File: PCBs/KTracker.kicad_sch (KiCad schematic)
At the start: 63 parts, among them J1 Conn_01x02_Female, J2 Conn_01x04_Female, J3 Conn_01x02_Female, J4 Conn_01x08_Female, J5 Conn_01x02_Female, P1 USB_C_Plug_USB2.0, SW1 Option/FLASH Switch, SW2 Cali Switch, SW3 SW_SPDT MAIN POWER, U1 ME6211C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

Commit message: #auto_saved_files#
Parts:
- added U?: MPU-9250, Sensor_Motion:InvenSense_QFN-24_3x3mm_P0.4mm, symbol Sensor_Motion:MPU-9250
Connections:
- net +3V3: no longer R11.1, R12.1
- net AUX_SCL: now also U?.7 (AUX_SCL); no longer U3.7 (AUX_SCL)
- net AUX_SDA: now also U?.21 (AUX_SDA); no longer U3.6 (AUX_SDA)
- net GND: now also U?.18 (GND), U?.20 (RESV_GND); no longer C8.2, U3.18 (GND)
- net SCL: now also U?.23 (SCL/SCLK); no longer U3.23 (SCL)
- net SDA: now also U?.24 (SDA/MOSI); no longer U3.24 (SDA)
- net at U3.10 (REGOUT): no longer C7.1
- net at U3.11 (FSYNC), U3.9 (AD0): no longer R16.1
- net at U3.20 (CPOUT): no longer C8.1
- new net: R16.1, U?.11 (FSYNC), U?.9 (AD0/MISO)
- new net: C7.1, U?.10 (REGOUT)
- new net: R11.1, R12.1, U?.13 (VDD), U?.22 (~{CS}), U?.8 (VDDIO)
- no-connect marks 33 -> 35
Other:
- moved on the sheet: C7, C8, R11, R12, R16

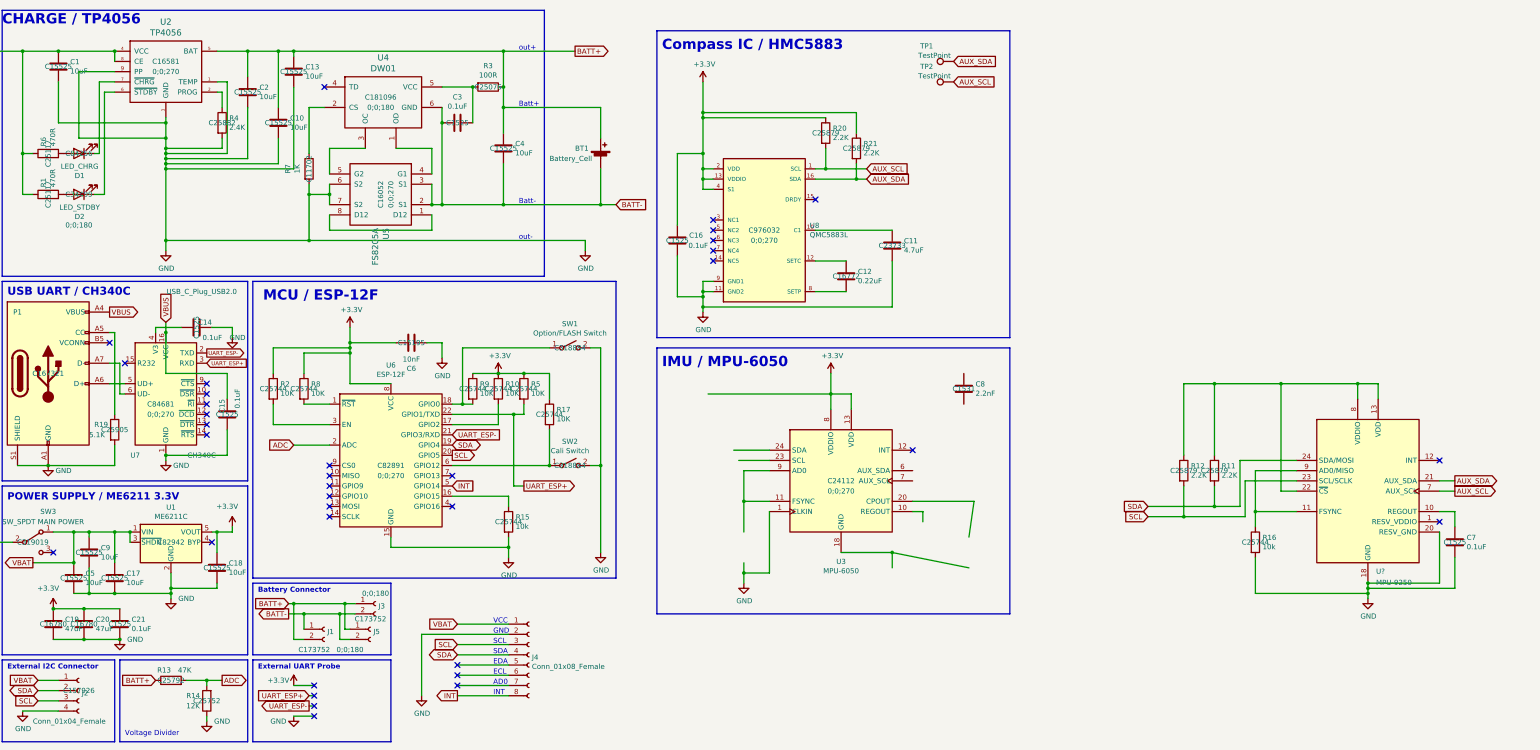
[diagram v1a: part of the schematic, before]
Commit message: MPU 6500!!
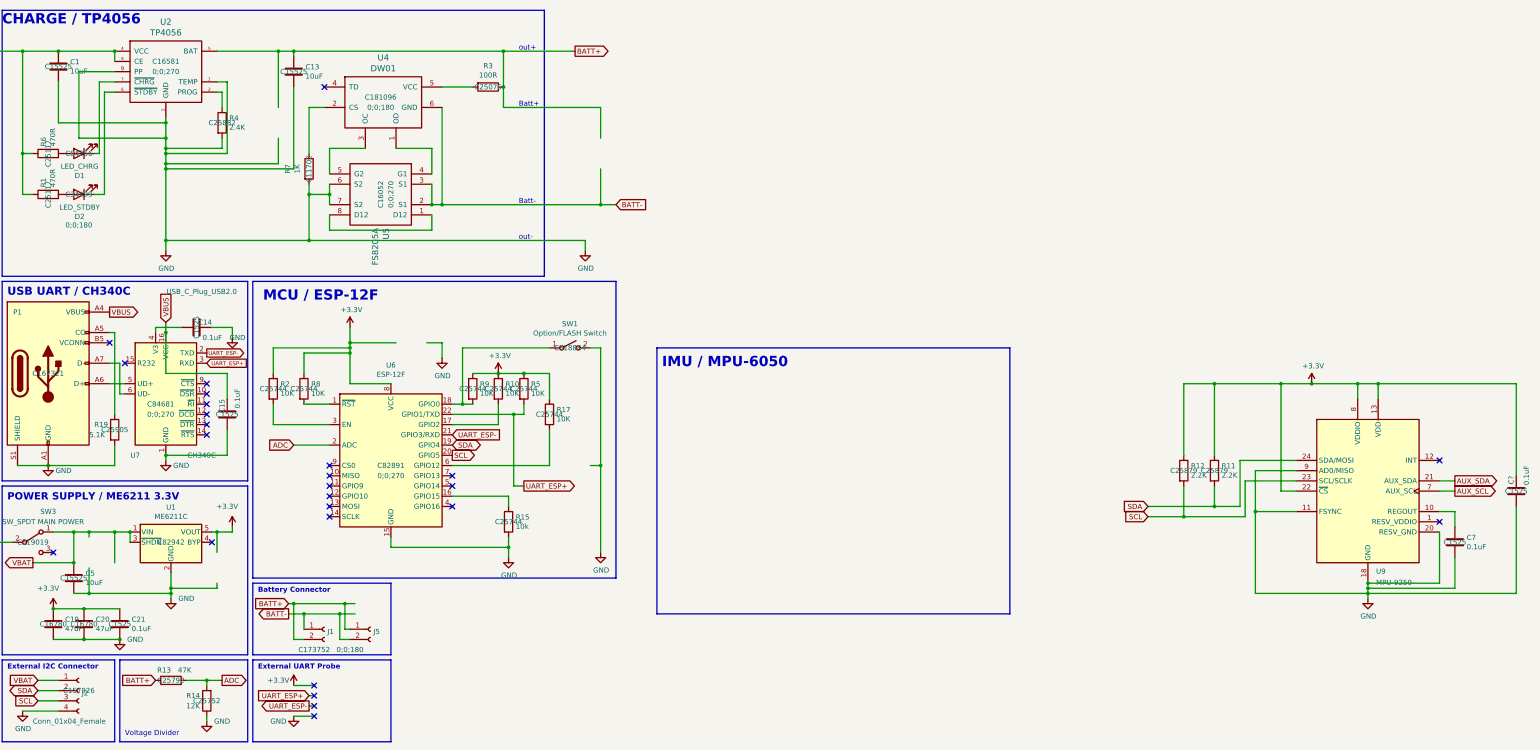
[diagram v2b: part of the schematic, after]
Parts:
- removed BT1: Battery_Cell, Battery:BatteryHolder_MPD_BH-18650-PC2, symbol Device:Battery_Cell
- removed C10, C17, C18, C2, C4, C9: 10uF, Capacitor_SMD:C_0402_1005Metric, symbol Device:C
- removed C11: 4.7uF, Capacitor_SMD:C_0402_1005Metric, symbol Device:C
- removed C12: 0.22uF, Capacitor_SMD:C_0402_1005Metric, symbol Device:C
- removed C16, C3: 0.1uF, Capacitor_SMD:C_0402_1005Metric, symbol Device:C
- removed C6: 10nF, Capacitor_SMD:C_0402_1005Metric, symbol Device:C
- removed C8: 2.2nF, Capacitor_SMD:C_0402_1005Metric, symbol Device:C
- removed J3: Conn_01x02_Female, Connector_JST:JST_PH_S2B-PH-K_1x02_P2.00mm_Horizontal, symbol Connector:Conn_01x02_Female
- removed J4: Conn_01x08_Female, Connector_PinSocket_2.54mm:PinSocket_1x08_P2.54mm_Vertical, symbol Connector:Conn_01x08_Female
- removed R16: 10k, Resistor_SMD:R_0402_1005Metric, symbol Device:R
- removed R20, R21: 2.2K, Resistor_SMD:R_0402_1005Metric, symbol Device:R
- removed SW2: Cali Switch, Button_Switch_SMD:SW_SPST_SKQG_WithoutStem, symbol Switch:SW_SPST
- removed TP1, TP2: TestPoint, TestPoint:TestPoint_Pad_D1.0mm, symbol Connector:TestPoint
- removed U3: MPU-6050, Sensor_Motion:InvenSense_QFN-24_4x4mm_P0.5mm, symbol Sensor_Motion:MPU-6050
- removed U8: QMC5883L, Package_LGA:LGA-16_3x3mm_P0.5mm, symbol HMC5883L:HMC5883L
- added C?: 0.1uF, Capacitor_SMD:C_0402_1005Metric, symbol Device:C
- SW1: footprint Button_Switch_SMD:SW_SPST_SKQG_WithoutStem -> mod_legacy:TS-1088R
- gave numbers to parts that had none: 1
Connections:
- net +3V3: now also R11.1, R12.1, U9.13 (VDD), U9.22 (~{CS}), U9.8 (VDDIO), C?.2
- net GND: now also U9.11 (FSYNC), U9.9 (AD0/MISO), C?.1
- net INT: no longer names the net of U6.5 (GPIO14)
- no-connect marks 35 -> 26
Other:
- note removed: "AD0"
- note removed: "Compass IC / HMC5883"
- note removed: "ECL"
- note removed: "EDA"
- note removed: "GND"
- note removed: "INT"
- note removed: "SCL"
- note removed: "SDA"
- note removed: "VCC"

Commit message: update
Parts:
- removed J5: Conn_01x02_Female, kami:MOLEX_532610271, symbol Connector:Conn_01x02_Female
- added TP1: Batt+, Connector_Pin:Pin_D0.9mm_L10.0mm_W2.4mm_FlatFork, symbol Connector:TestPoint
- added TP?: Batt-, Connector_Pin:Pin_D0.9mm_L10.0mm_W2.4mm_FlatFork, symbol Connector:TestPoint
- U4: footprint Package_TO_SOT_SMD:SOT-23-6_Handsoldering -> Package_TO_SOT_SMD:SOT-23-6
- gave numbers to parts that had none: 1
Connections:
- net BATT+: now also TP1.1
- net BATT-: now also TP?.1
- no-connect marks 26 -> 28
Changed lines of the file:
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@@
   (junction (at 99.06 71.12) (diameter 0) (color 0 0 0 0)
+  )
+  (junction (at 139.7 33.02) (diameter 0) (color 0 0 0 0)
   )
   (junction (at 323.85 137.16) (diameter 0) (color 0 0 0 0)
@@
   (no_connect (at 379.73 125.73))
   (no_connect (at 100.33 181.61))
+  (no_connect (at 109.22 167.64))
   (no_connect (at 73.66 109.22))
   (no_connect (at 100.33 184.15))
@@
   (no_connect (at 73.66 111.76))
   (no_connect (at 134.62 129.54))
+  (no_connect (at 109.22 170.18))
   (no_connect (at 134.62 132.08))
   (no_connect (at 35.56 148.59))
@@
     (stroke (width 0) (type default) (color 0 0 0 0))
   )
+  (wire (pts (xy 139.7 41.91) (xy 139.7 33.02))
+    (stroke (width 0) (type default) (color 0 0 0 0))
+  )
   (wire (pts (xy 139.7 33.02) (xy 132.08 33.02))
     (stroke (width 0) (type default) (color 0 0 0 0))
@@
     (stroke (width 0) (type default) (color 0 0 0 0))
   )
+  (wire (pts (xy 132.08 38.1) (xy 132.08 62.23))
+    (stroke (width 0) (type default) (color 0 0 0 0))
+  )
   (wire (pts (xy 76.2 24.13) (xy 91.44 24.13))
     (stroke (width 0) (type default) (color 0 0 0 0))
@@
   )
   (polyline (pts (xy 175.26 81.28) (xy 175.26 154.94))
-    (stroke (width 0) (type default) (color 0 0 0 0))
-  )
-  (wire (pts (xy 132.08 38.1) (xy 132.08 62.23))
     (stroke (width 0) (type default) (color 0 0 0 0))
   )
@@
       (effects (font (size 1.524 1.524)))
     )
-    (property "Footprint" "Package_TO_SOT_SMD:SOT-23-6_Handsoldering" (id 2) (at 115.57 44.45 0)
+    (property "Footprint" "Package_TO_SOT_SMD:SOT-23-6" (id 2) (at 115.57 44.45 0)
       (effects (font (size 1.524 1.524)) hide)
     )
@@
     )
     (property "LCSC" "C15525" (id 4) (at 40.64 154.94 0))
-    (pin "1")
-    (pin "2")
-  )
-  (symbol (lib_id "Connector:Conn_01x02_Female") (at 114.3 167.64 0) (unit 1)
-    (in_bom yes) (on_board yes)
-    (property "Reference" "J5" (id 0) (at 115.0112 168.2496 0)
-      (effects (font (size 1.27 1.27)) (justify left))
-    )
-    (property "Value" "Conn_01x02_Female" (id 1) (at 104.14 171.45 0)
-      (effects (font (size 1.27 1.27)) (justify left) hide)
-    )
-    (property "Footprint" "kami:MOLEX_532610271" (id 2) (at 114.3 167.64 0)
-      (effects (font (size 1.27 1.27)) hide)
-    )
-    (property "Datasheet" "~" (id 3) (at 114.3 167.64 0)
-      (effects (font (size 1.27 1.27)) hide)
-    )
     (pin "1")
     (pin "2")
@@
     (pin "1")
   )
+  (symbol (lib_id "Connector:TestPoint") (at 110.49 163.83 270) (unit 1)
+    (in_bom yes) (on_board yes)
+    (property "Reference" "TP?" (id 0) (at 115.189 162.9215 90)
+      (effects (font (size 1.27 1.27)) (justify left))
+    )
+    (property "Value" "Batt-" (id 1) (at 107.95 162.56 90)
+      (effects (font (size 1.27 1.27)) (justify left))
+    )
+    (property "Footprint" "Connector_Pin:Pin_D0.9mm_L10.0mm_W2.4mm_FlatFork" (id 2) (at 110.49 168.91 0)
+      (effects (font (size 1.27 1.27)) hide)
+    )
+    (property "Datasheet" "~" (id 3) (at 110.49 168.91 0)
+      (effects (font (size 1.27 1.27)) hide)
+    )
+    (pin "1")
+  )
+  (symbol (lib_id "Connector:TestPoint") (at 110.49 161.29 270) (unit 1)
+    (in_bom yes) (on_board yes)
+    (property "Reference" "TP1" (id 0) (at 115.189 160.3815 90)
+      (effects (font (size 1.27 1.27)) (justify left))
+    )
+    (property "Value" "Batt+" (id 1) (at 107.95 160.02 90)
+      (effects (font (size 1.27 1.27)) (justify left))
+    )
+    (property "Footprint" "Connector_Pin:Pin_D0.9mm_L10.0mm_W2.4mm_FlatFork" (id 2) (at 110.49 166.37 0)
+      (effects (font (size 1.27 1.27)) hide)
+    )
+    (property "Datasheet" "~" (id 3) (at 110.49 166.37 0)
+      (effects (font (size 1.27 1.27)) hide)
+    )
+    (pin "1")
+  )
   (symbol (lib_id "Sensor_Motion:MPU-9250") (at 361.95 133.35 0) (unit 1)
     (in_bom yes) (on_board yes) (fields_autoplaced)
@@
   (symbol (lib_id "Device:C") (at 398.78 133.35 180) (unit 1)
     (in_bom yes) (on_board yes)
-    (property "Reference" "C?" (id 0) (at 397.51 129.54 90)
+    (property "Reference" "C2" (id 0) (at 397.51 129.54 90)
       (effects (font (size 1.27 1.27)) (justify left))
     )
@@
       (reference "C1") (unit 1) (value "10uF") (footprint "Capacitor_SMD:C_0402_1005Metric")
     )
+    (path "/fd86d1a8-79f8-4d1e-a799-876f7cb19eef"
+      (reference "C2") (unit 1) (value "0.1uF") (footprint "Capacitor_SMD:C_0402_1005Metric")
+    )
     (path "/00000000-0000-0000-0000-000061f70f64"
       (reference "C5") (unit 1) (value "10uF") (footprint "Capacitor_SMD:C_0402_1005Metric")
@@
       (reference "C21") (unit 1) (value "0.1uF") (footprint "Capacitor_SMD:C_0402_1005Metric")
     )
-    (path "/fd86d1a8-79f8-4d1e-a799-876f7cb19eef"
-      (reference "C?") (unit 1) (value "0.1uF") (footprint "Capacitor_SMD:C_0402_1005Metric")
-    )
     (path "/00000000-0000-0000-0000-0000614c3d7e"
       (reference "D1") (unit 1) (value "LED_CHRG") (footprint "LED_SMD:LED_0805_2012Metric")
@@
       (reference "J2") (unit 1) (value "Conn_01x04_Female") (footprint "Connector_JST:JST_PH_S4B-PH-K_1x04_P2.00mm_Horizontal")
     )
-    (path "/00000000-0000-0000-0000-0000620aed9a"
-      (reference "J5") (unit 1) (value "Conn_01x02_Female") (footprint "kami:MOLEX_532610271")
-    )
     (path "/00000000-0000-0000-0000-00006222078b"
       (reference "P1") (unit 1) (value "USB_C_Plug_USB2.0") (footprint "Connector_USB:USB_C_Receptacle_HRO_TYPE-C-31-M-12")
@@
       (reference "SW3") (unit 1) (value "SW_SPDT MAIN POWER") (footprint "Button_Switch_SMD:SW_SPDT_PCM12")
     )
+    (path "/9694d1dc-c04e-48c6-a866-c6c6f119dae7"
+      (reference "TP1") (unit 1) (value "Batt+") (footprint "Connector_Pin:Pin_D0.9mm_L10.0mm_W2.4mm_FlatFork")
+    )
+    (path "/7474922a-d357-4fbb-9452-85c134f4f49e"
+      (reference "TP?") (unit 1) (value "Batt-") (footprint "Connector_Pin:Pin_D0.9mm_L10.0mm_W2.4mm_FlatFork")
+    )
     (path "/00000000-0000-0000-0000-000062335044"
       (reference "U1") (unit 1) (value "ME6211C") (footprint "Package_TO_SOT_SMD:SOT-23-5")
@@
     )
     (path "/00000000-0000-0000-0000-0000614edb03"
-      (reference "U4") (unit 1) (value "DW01") (footprint "Package_TO_SOT_SMD:SOT-23-6_Handsoldering")
+      (reference "U4") (unit 1) (value "DW01") (footprint "Package_TO_SOT_SMD:SOT-23-6")
     )
     (path "/00000000-0000-0000-0000-0000614f31c6"

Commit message: 완성!
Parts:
- added C10: 10uF, Capacitor_SMD:C_0402_1005Metric, symbol Device:C
- gave numbers to parts that had none: 1
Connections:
- net BATT+: now also C10.1
- net GND: now also C10.2
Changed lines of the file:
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@@
     (pin "1")
+  )
+  (symbol (lib_id "Device:C") (at 91.44 41.91 0) (unit 1)
+    (in_bom yes) (on_board yes)
+    (property "Reference" "C10" (id 0) (at 94.361 40.7416 0)
+      (effects (font (size 1.27 1.27)) (justify left))
+    )
+    (property "Value" "10uF" (id 1) (at 94.361 43.053 0)
+      (effects (font (size 1.27 1.27)) (justify left))
+    )
+    (property "Footprint" "Capacitor_SMD:C_0402_1005Metric" (id 2) (at 92.4052 45.72 0)
+      (effects (font (size 1.27 1.27)) hide)
+    )
+    (property "Datasheet" "~" (id 3) (at 91.44 41.91 0)
+      (effects (font (size 1.27 1.27)) hide)
+    )
+    (property "LCSC" "C15525" (id 4) (at 91.44 41.91 0))
+    (pin "1")
+    (pin "2")
   )
   (symbol (lib_id "Connector:TestPoint") (at 110.49 163.83 270) (unit 1)
     (in_bom yes) (on_board yes)
-    (property "Reference" "TP?" (id 0) (at 115.189 162.9215 90)
+    (property "Reference" "TP2" (id 0) (at 115.189 162.9215 90)
       (effects (font (size 1.27 1.27)) (justify left))
     )
@@
       (reference "C7") (unit 1) (value "0.1uF") (footprint "Capacitor_SMD:C_0402_1005Metric")
     )
+    (path "/5401772f-eac2-49f8-aab3-944b0ada781c"
+      (reference "C10") (unit 1) (value "10uF") (footprint "Capacitor_SMD:C_0402_1005Metric")
+    )
     (path "/00000000-0000-0000-0000-0000620f28e9"
       (reference "C13") (unit 1) (value "10uF") (footprint "Capacitor_SMD:C_0402_1005Metric")
@@
     )
     (path "/7474922a-d357-4fbb-9452-85c134f4f49e"
-      (reference "TP?") (unit 1) (value "Batt-") (footprint "Connector_Pin:Pin_D0.9mm_L10.0mm_W2.4mm_FlatFork")
+      (reference "TP2") (unit 1) (value "Batt-") (footprint "Connector_Pin:Pin_D0.9mm_L10.0mm_W2.4mm_FlatFork")
     )
     (path "/00000000-0000-0000-0000-000062335044"

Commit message: !
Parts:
- removed R3: 100R, Resistor_SMD:R_0402_1005Metric, symbol Device:R
- removed R7: 1K, Resistor_SMD:R_0402_1005Metric, symbol Device:R
- removed U4: DW01, Package_TO_SOT_SMD:SOT-23-6, symbol dw01:DW01
- removed U5: FS8205A, Package_SO:TSSOP-8_4.4x3mm_P0.65mm, symbol fs8205a:FS8205A
- U9: LCSC (none) -> C50278
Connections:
- net BATT- is gone; now on net GND: J1.1 (Pin_1), TP2.1
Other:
- moved on the sheet: C2, C7, R11, R12, U9

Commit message: clear silk
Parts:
- SW1: LCSC C318884 -> C455280
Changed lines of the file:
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@@
       (effects (font (size 1.27 1.27)) hide)
     )
-    (property "LCSC" "C318884" (id 4) (at 163.83 97.79 0))
+    (property "LCSC" "C455280" (id 4) (at 163.83 97.79 0))
     (pin "1")
     (pin "2")

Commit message: yay
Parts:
- U9: JLCPCB_CORRECTION (none) -> 0;0;270
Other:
- company: github.com/Kamilake/KamiTrack-SlimeVR-PCB -> github.com/Kamilake/KTracker-SlimeVR-PCB
- title: KamiTrack-SlimeVR-PCB -> KTracker-SlimeVR-PCB
- moved on the sheet: C2, C7, R11, R12, U9

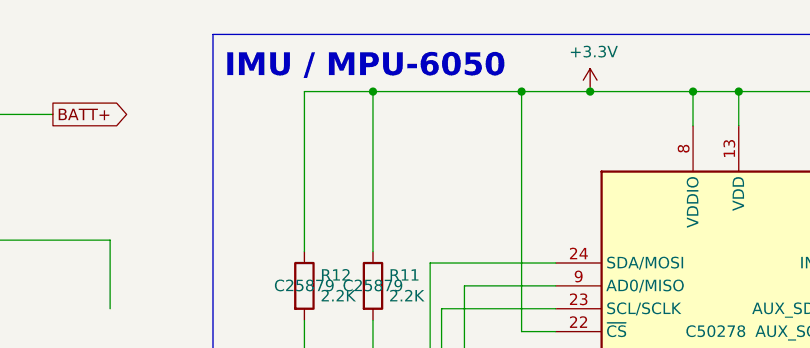
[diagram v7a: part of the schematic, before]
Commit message: 6050->6500
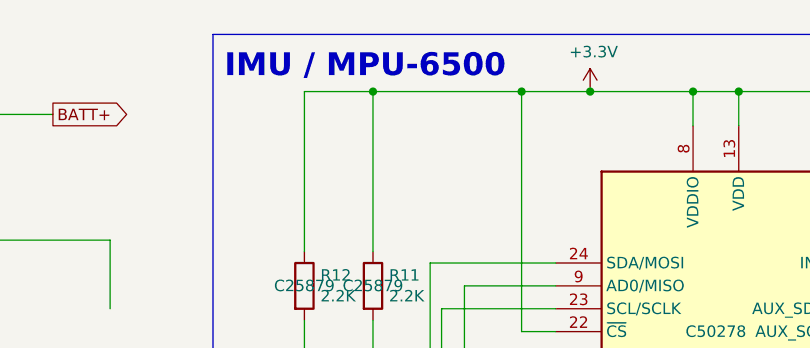
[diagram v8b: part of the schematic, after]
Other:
- note added: "IMU / MPU-6500"
- note removed: "IMU / MPU-6050"
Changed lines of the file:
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@@
     (effects (font (size 1.27 1.27) (thickness 0.254) bold) (justify left bottom))
   )
-  (text "IMU / MPU-6050" (at 184.15 20.32 0)
+  (text "IMU / MPU-6500" (at 184.15 20.32 0)
     (effects (font (size 2.54 2.54) (thickness 0.508) bold) (justify left bottom))
   )
